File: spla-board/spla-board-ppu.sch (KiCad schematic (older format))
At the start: 31 parts, among them J8 J_PPURESET, J9 J_DPULL, U10 SNES_PPU1, U11 SNES_PPU2, U12 VRAM, U13 VRAM

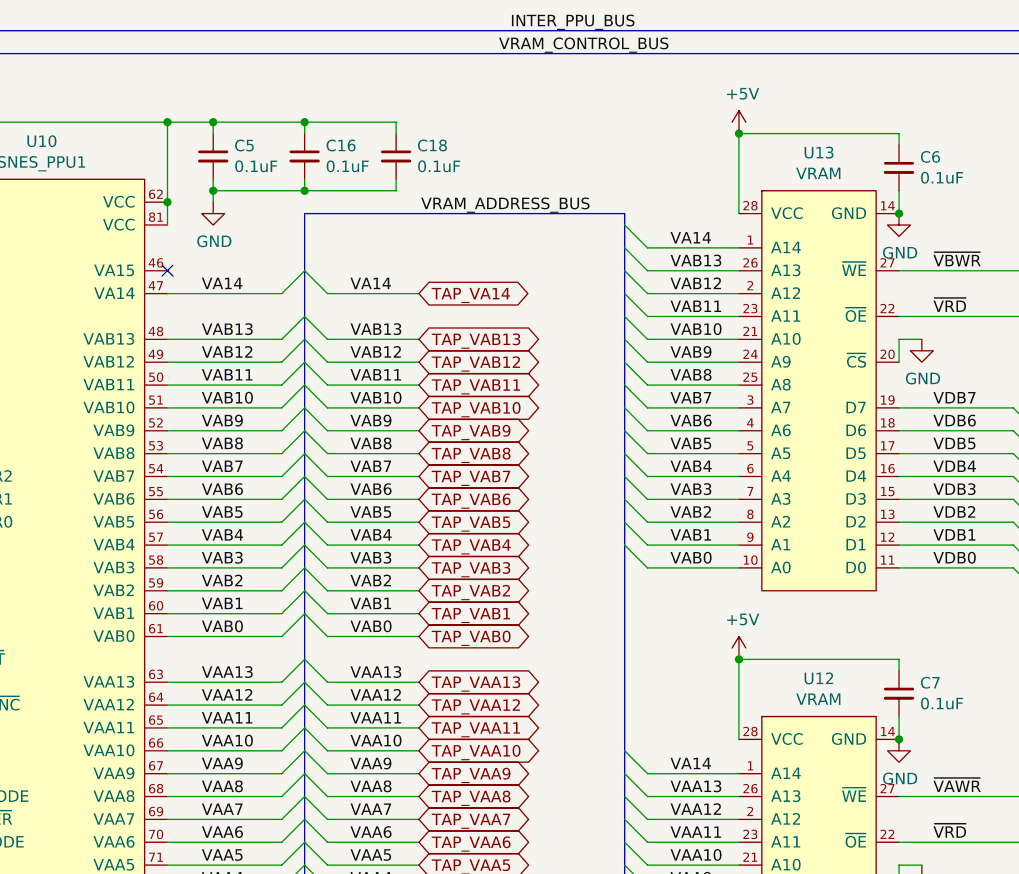
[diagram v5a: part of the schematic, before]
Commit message: schematic/pcb: Label a few more nets properly.
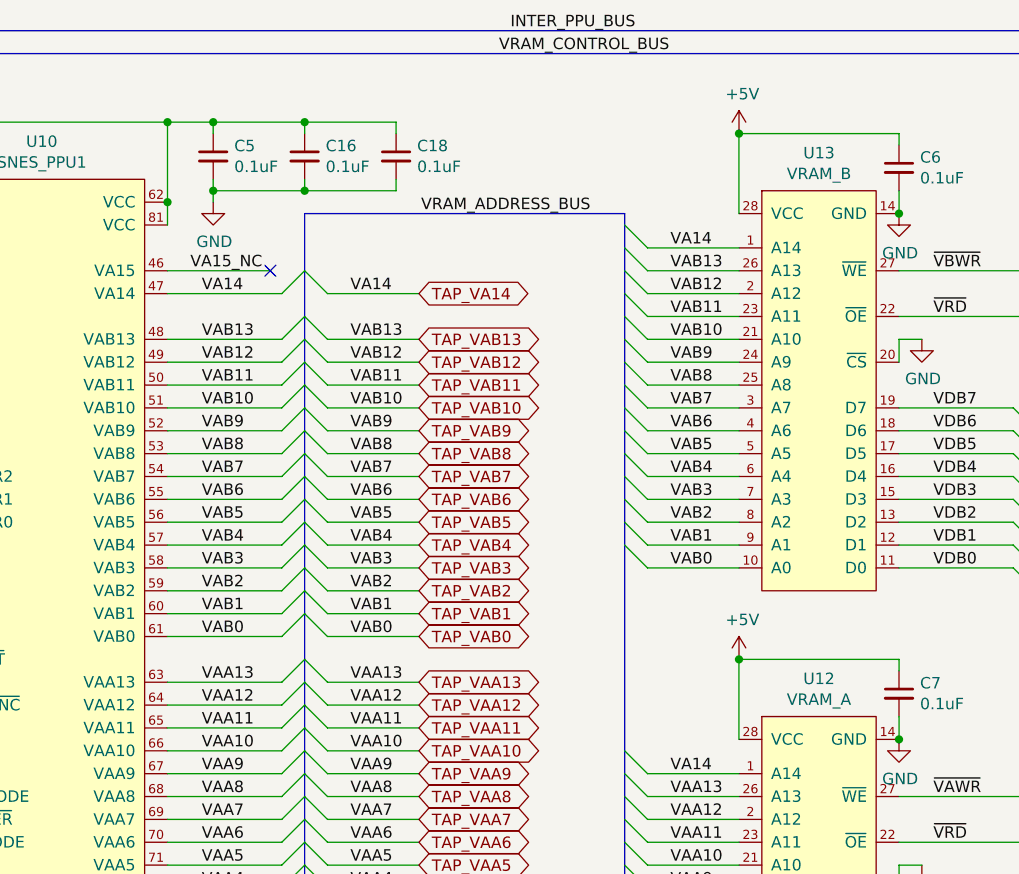
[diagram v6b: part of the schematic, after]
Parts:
- U12: value VRAM -> VRAM_A
- U13: value VRAM -> VRAM_B
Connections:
- net VA15_NC: now reaches U10.46 (VA15)
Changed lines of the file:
@@
 AR Path="/5E50E589/5E55B6D1" Ref="U13"  Part="1"
 F 0 "U13" H 9050 4965 50  0000 C CNN
-F 1 "VRAM" H 9050 4874 50  0000 C CNN
+F 1 "VRAM_B" H 9050 4874 50  0000 C CNN
 F 2 "SPLA:SOP-28_17x8mm_P1.27mm" H 9050 4050 50  0001 C CNN
 F 3 "" H 9050 4050 50  0001 C CNN
@@
 AR Path="/5E50E589/5E55C6FE" Ref="U12"  Part="1"
 F 0 "U12" H 9050 7265 50  0000 C CNN
-F 1 "VRAM" H 9050 7174 50  0000 C CNN
+F 1 "VRAM_A" H 9050 7174 50  0000 C CNN
 F 2 "SPLA:SOP-28_17x8mm_P1.27mm" H 9050 6350 50  0001 C CNN
 F 3 "" H 9050 6350 50  0001 C CNN
@@
 Wire Wire Line
 	8700 5850 8300 5850
-NoConn ~ 6200 3650
 Entry Wire Line
 	8200 4850 8300 4950
@@
 	1    0    0    -1
 $EndComp
-$Comp
-L power:GND #PWR0128
-U 1 1 5EEE50C6
-P 9500 6250
-F 0 "#PWR0128" H 9500 6000 50  0001 C CNN
-F 1 "GND" H 9505 6077 50  0000 C CNN
-F 2 "" H 9500 6250 50  0001 C CNN
-F 3 "" H 9500 6250 50  0001 C CNN
-	1    9500 6250
-	1    0    0    -1
-$EndComp
 Wire Wire Line
 	9400 4050 9400 3950
 Wire Wire Line
-	9400 3950 9500 3950
-Wire Wire Line
 	9400 6350 9400 6250
-Wire Wire Line
-	9400 6250 9500 6250
 Text Label 9550 5950 0    50   ~ 0
 ~VAWR
@@
 Connection ~ 14250 4150
 $Comp
-L power:PWR_FLAG #FLG?
+L power:PWR_FLAG #FLG0109
 U 1 1 603660AC
 P 14600 4150
-F 0 "#FLG?" H 14600 4225 50  0001 C CNN
+F 0 "#FLG0109" H 14600 4225 50  0001 C CNN
 F 1 "PWR_FLAG" H 14600 4323 50  0000 C CNN
 F 2 "" H 14600 4150 50  0001 C CNN
@@
 Wire Wire Line
 	14600 4150 14950 4150
+Wire Wire Line
+	6200 3650 6650 3650
+Text Label 6300 3650 0    50   ~ 0
+VA15_NC
+NoConn ~ 6650 3650
+Wire Wire Line
+	9400 3950 9500 3950
 Wire Bus Line
 	10200 2700 10200 6050
@@
 	3350 2700 3350 6550
 Wire Bus Line
-	4550 2600 4550 5150
+	6800 7050 6800 9400
 Wire Bus Line
-	10850 2600 10850 5450
+	13350 6150 13350 9400
 Wire Bus Line
-	6800 7050 6800 9400
+	10000 4350 10000 9400
 Wire Bus Line
 	11100 6950 11100 9500
@@
 	4550 6950 4550 9500
 Wire Bus Line
-	6800 3400 6800 6650
+	10850 2600 10850 5450
 Wire Bus Line
 	8200 3400 8200 7150
 Wire Bus Line
-	13350 6150 13350 9400
+	6800 3400 6800 6650
 Wire Bus Line
-	10000 4350 10000 9400
+	4550 2600 4550 5150
+Wire Wire Line
+	9400 6250 9500 6250
+$Comp
+L power:GND #PWR0128
+U 1 1 5EEE50C6
+P 9500 6250
+F 0 "#PWR0128" H 9500 6000 50  0001 C CNN
+F 1 "GND" H 9505 6077 50  0000 C CNN
+F 2 "" H 9500 6250 50  0001 C CNN
+F 3 "" H 9500 6250 50  0001 C CNN
+	1    9500 6250
+	1    0    0    -1
+$EndComp
 $EndSCHEMATC
